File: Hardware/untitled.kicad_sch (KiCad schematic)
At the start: 18 parts

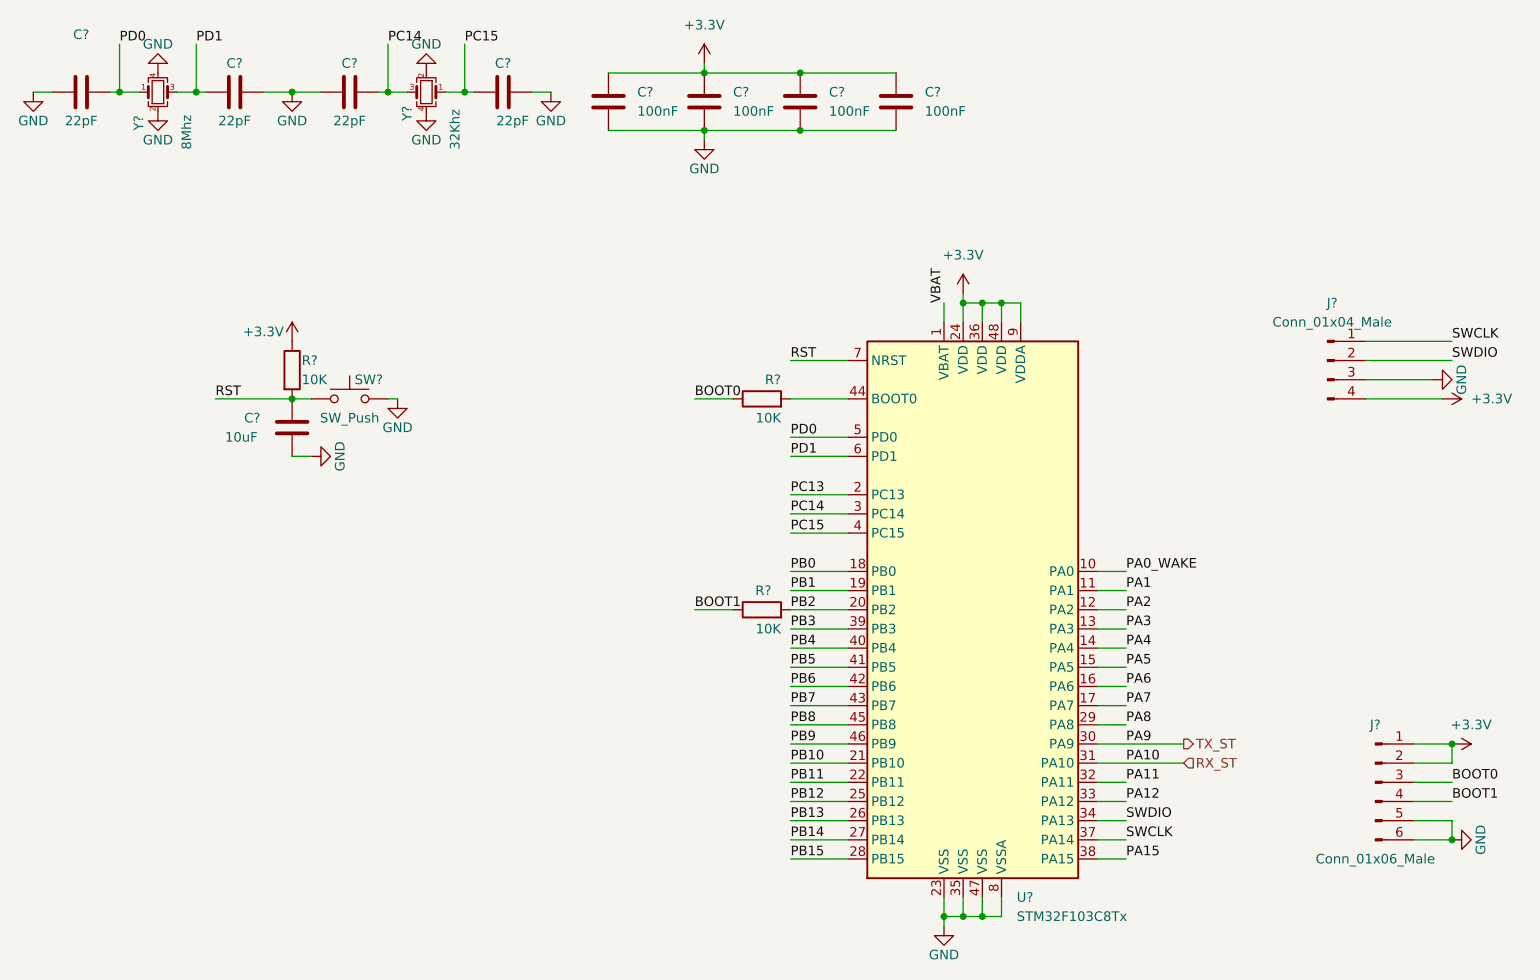
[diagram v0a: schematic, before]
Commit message: complete sch ESP32, Power, eeprom
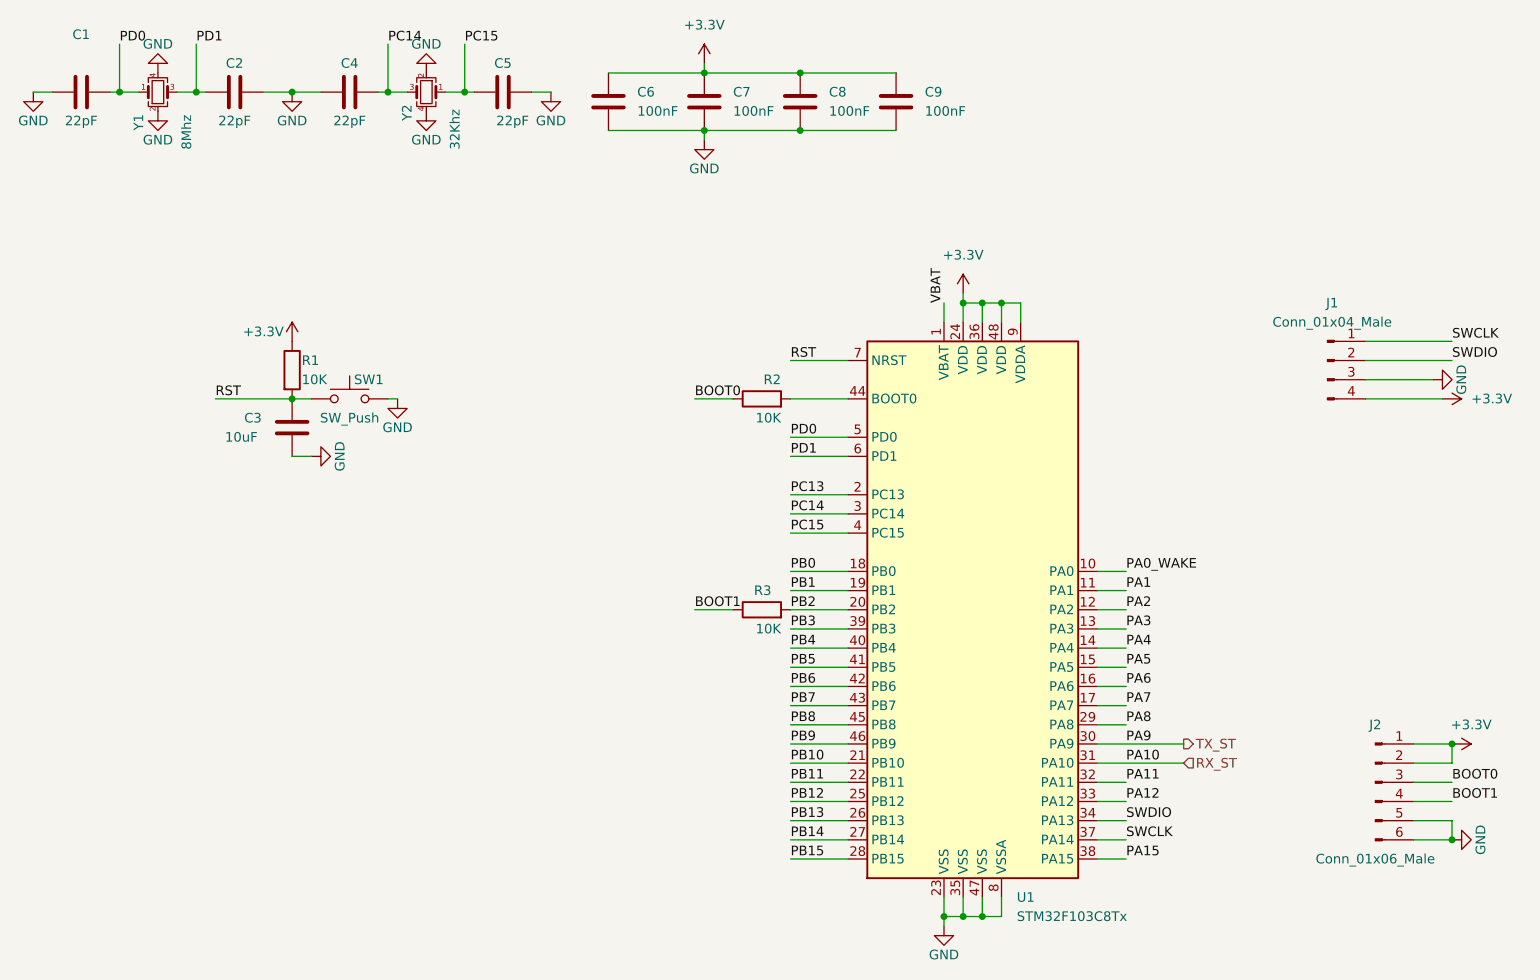
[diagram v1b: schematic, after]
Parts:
- J1: renamed from J?; footprint (none) -> Connector_PinHeader_2.54mm:PinHeader_1x04_P2.54mm_Vertical
- gave numbers to parts that had none: 17
